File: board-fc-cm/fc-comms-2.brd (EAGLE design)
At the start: 95.9 x 90.2 mm, 230 parts, among them IC1 TPS79930QDDCRQ1, IC11 MPU-9250, IC12 TXB0108PW, IC13 TPS3813K33-EP_DBV_6, IC14 TMP100-EP_DBV_6, IC15 LHA1+, IC16 PCT2075TP, IC17 MMZ09332BT1, IC18 PCT2075TP, IC2 TPS79930QDDCRQ1, IC3 MSP430FR2311PW, IC4 MCP1700TT, IC5 TXB0108PW, IC6 TXB0108PW, IC7 CC1125RHBT, IC77 74LVC1G08, IC8 CC1125RHBT, IC9 TM4C123[7,G]XXPM, J3 SWD_SHROUD, Q3 32.768kHz, Q4 BSS123, Q5 BSS84, X1 SHIELD-26X26, X12 BU-SMA-V, X18 BU-SMA-V, X2 SHIELD-26X26, X3 LFTCXO070, X4 LFTCXO070, X5 SHIELD-26X26, X6 SHIELD-26X26, Y1 8MHz

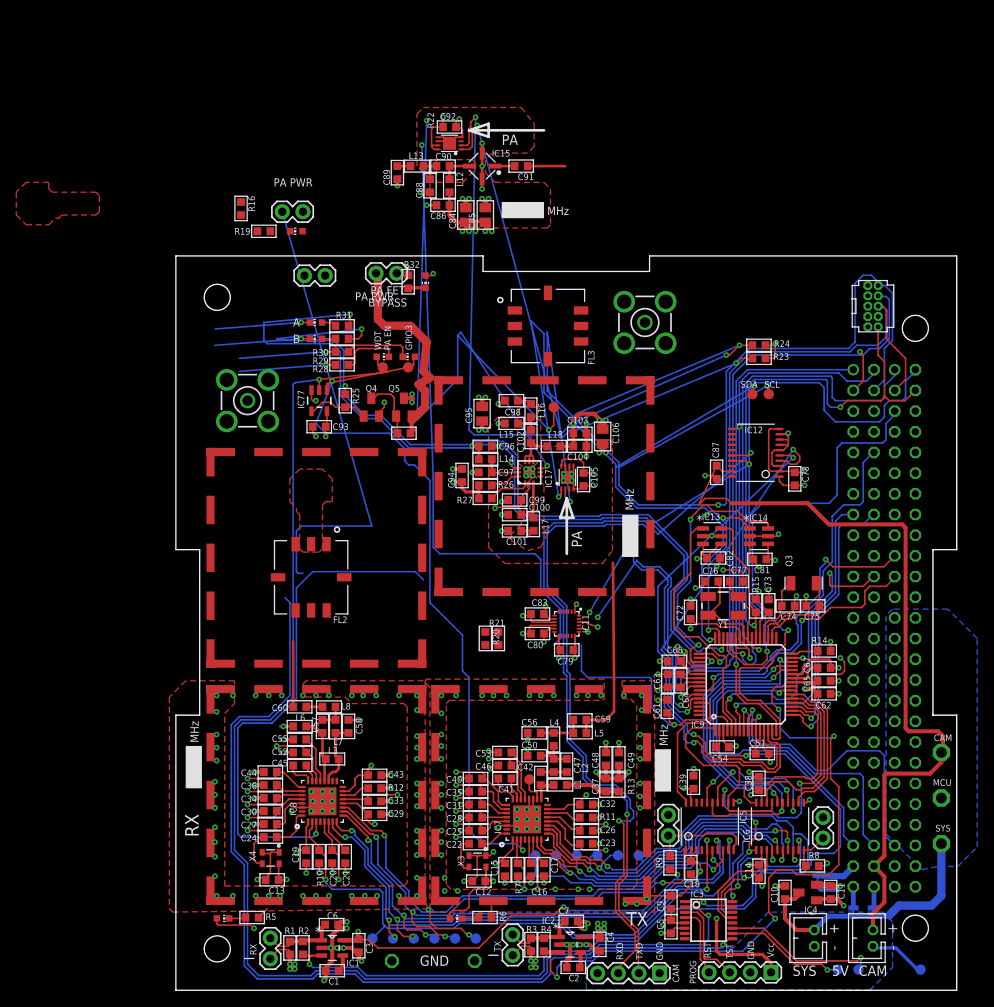
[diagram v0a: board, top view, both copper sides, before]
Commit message: adding fram, some routing
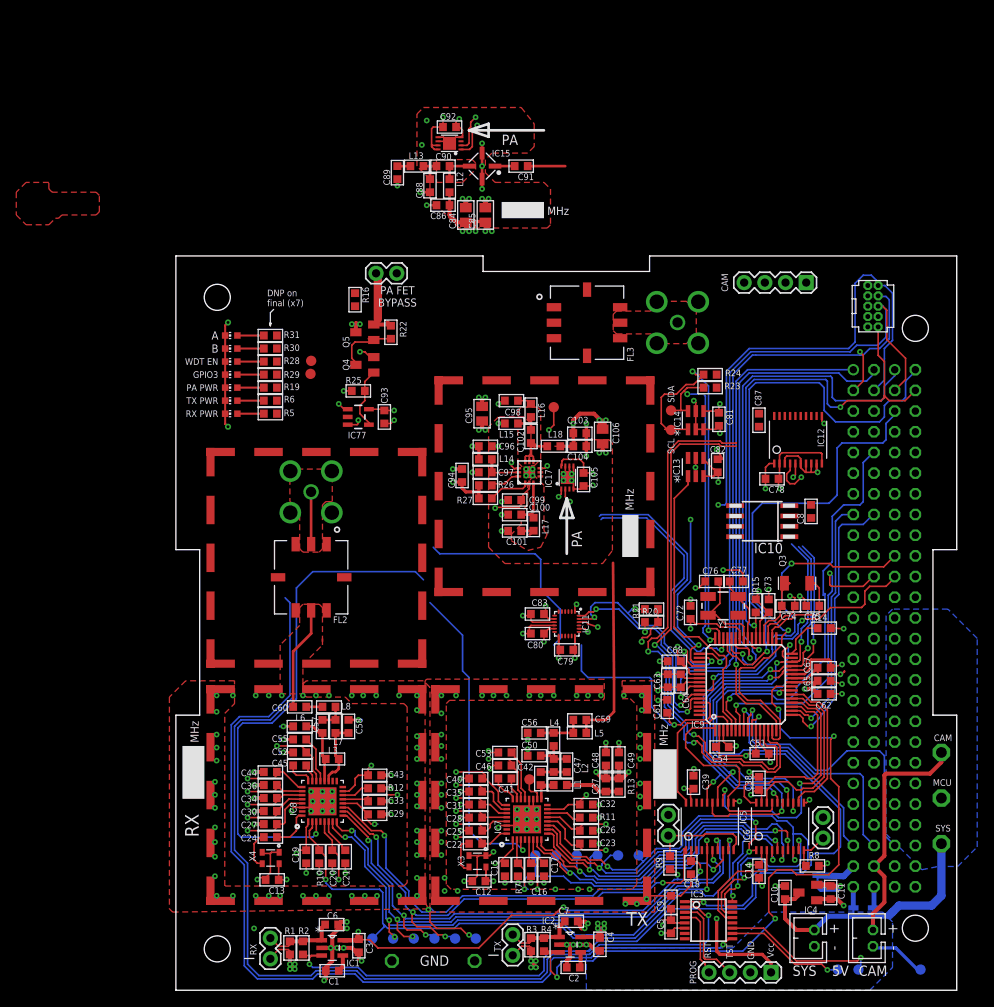
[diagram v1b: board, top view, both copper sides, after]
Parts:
- removed JP11, JP9: M02PTH, SparkFun-Connectors:1X02
- removed LED9: (no value), dtb:CHIP-LED0603
- removed R32: (no value), passives-7351:R0603-N
- added C8: 0.1u, passives-7351:C0603-N
- added IC10: FM25V10, cube-parts:SO-08M
- moved JP12 86.7 mm to (77.4, 86.9)
- moved LED1 69.3 mm to (6.80, 72.4), turned to 90 degrees
- moved R6 68.7 mm to (11.6, 72.4), turned to 180 degrees
- moved LED2 62.0 mm to (6.80, 70.8), turned to 90 degrees
- moved R5 61.9 mm to (11.6, 70.8), turned to 180 degrees
- moved LED6 21.9 mm to (6.80, 75.6)
- moved LED4 20.8 mm to (6.80, 74.0)
- moved R20 20.5 mm to (58.4, 45.2), turned to 0 degrees
- moved R19 19.2 mm to (11.6, 74.0), turned to 180 degrees
- moved R21 19.1 mm to (58.4, 46.8), turned to 0 degrees
- moved LED5 18.6 mm to (6.80, 77.2), turned to 90 degrees
- moved R16 17.9 mm to (22.0, 84.8)
- moved C81 17.9 mm to (66.7, 70.1), turned to 270 degrees
- moved IC14 16.2 mm to (63.8, 70.0), turned to 90 degrees
- moved X12 13.6 mm to (16.6, 61.2), flipped to the bottom
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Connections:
- removed net N$101: C60.2
- removed net N$24: C103.1, C104.1, C106.1, C94.1, C95.1, C96.1, C99.1, IC17.2, JP11.1, L14.2, L18.2, LED9.A, R26.1, R27.1
- removed net N$66: LED1.C, R6.1
- removed net N$67: LED2.C, R5.1
- removed net N$83: C84.1, C85.1, C86.2, JP9.1, L12.2, LED4.A
- removed net N$84: LED4.C, R19.1
- removed net N$85: LED9.C, R32.1
- new net FRAM_CS: IC10.1, IC9.53
- new net N$10: LED5.A, R28.1
- new net N$25: LED6.A, R29.1
- new net N$46: LED2.A, R5.2
- net 3V3/FMCU: now also C8.1, IC10.3, IC10.7, IC10.8
- net GND: now also C8.2, IC10.4, LED1.C, LED2.C, LED4.C, LED5.C, LED6.C; no longer R19.2, R28.1, R29.1, R32.2, R5.2, R6.2
- net N$38: now also LED4.A, R19.2; no longer LED5.C, R28.2
- net N$40: now also R6.1; no longer LED1.A
- net N$41: now also LED1.A, R6.2; no longer LED6.C, R29.2
- net N$53: now also R5.1; no longer LED2.A
- net N$56: now also C60.2
- net PA_PWR: now also C103.1, C104.1, C106.1, C84.1, C85.1, C86.2, C94.1, C95.1, C96.1, C99.1, IC17.2, L12.2, L14.2, L18.2, R19.1, R26.1, R27.1; no longer JP11.2, JP9.2
- net TC/TXRX/CLK: now also IC10.6
- net TC/TXRX/MISO: now also IC10.2
- net TC/TXRX/MOSI: now also IC10.5
- net TX_GPIO3: now also R29.2; no longer LED6.A
- net WDT_PA_EN: now also R28.2; no longer LED5.A
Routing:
- net TMP/SCL: track 206.5 -> 57.0 mm, vias 7 -> 4
- net PA_POWER: track 275.7 -> 140.8 mm
- net TMP/SDA: track 179.8 -> 46.7 mm, vias 6 -> 4
- net N$83: track 104.2 -> 0.00 mm, vias 5 -> 0
- net N$73: track 94.2 -> 0.00 mm, vias 2 -> 0
- net N$61: track 94.1 -> 0.00 mm, vias 2 -> 0
- net PA_PWR: track 72.8 -> 166.2 mm, vias 2 -> 14
- net N$24: track 89.3 -> 0.00 mm, vias 9 -> 1
- net N$49: track 103.5 -> 31.4 mm, vias 2 -> 1
- net N$51: track 100.3 -> 31.4 mm, vias 2 -> 1
- net 5V/CAM: track 95.9 -> 29.5 mm
- net GND: track 999.0 -> 1055.8 mm, vias 236 -> 232
- net WDT_PA_EN: track 159.8 -> 105.7 mm, vias 2 -> 1
- net TX_GPIO3: track 91.7 -> 40.6 mm
- net 5V/TX: track 38.4 -> 19.5 mm
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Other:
- board text added: "Comms/FC Board V.2"
- board text added: "DNP on final (x7)"
- board text added: "RX PWR"
- board text added: "TX PWR"
- board text added: "WDT EN"
- board text removed: "Comms/FC Development Board V.1"
- board text removed: "WDT PA EN"

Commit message: most routing done, still some queries remain
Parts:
- moved R16 1.26 mm to (22.4, 83.6), turned to 180 degrees
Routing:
- net GND: track 1055.8 -> 416.6 mm, vias 232 -> 234
- net 3V3/FMCU: track 288.4 -> 157.2 mm, vias 18 -> 21
- net PA_PWR: track 166.2 -> 71.6 mm, vias 14 -> 15
- net PA_POWER: track 140.8 -> 52.7 mm
- net N$51: track 31.4 -> 98.0 mm, vias 1 -> 2
- net N$49: track 31.4 -> 96.2 mm, vias 1 -> 2
- net RX_GPIO3: track 63.6 -> 1.53 mm
- net WDT_PA_EN: track 105.7 -> 164.5 mm, vias 1 -> 2
- net N$53: track 149.4 -> 192.9 mm, vias 18 -> 19
- net N$1: track 115.6 -> 158.4 mm, vias 1 -> 2
- net FRAM_CS: track 0.00 -> 42.6 mm, vias 0 -> 2
- net TX_GPIO3: track 40.6 -> 80.9 mm, vias 2 -> 3
- net TMP/SDA: track 46.7 -> 66.4 mm, vias 4 -> 6
- net TMP/SCL: track 57.0 -> 76.2 mm, vias 4 -> 6
- net 5V/CAM: track 29.5 -> 47.0 mm
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- added copper zone on layer 1, net 5V/CAM
- added copper zone on layer 1, net N$2
- removed copper zone on layer 16, net 5V/CAM
- removed copper zone on layer 15, net N$2
- removed copper zone on layer 15, net N$24

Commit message: added camera header, RF connectors, some cleanup
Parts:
- removed JP12: (no value), SparkFun-Connectors:1X04
- removed JP13, JP14, JP4: JUMPER-SMT_2_NC_TRACE_SILK, SparkFun-Jumpers:SMT-JUMPER_2_NC_TRACE_SILK
- removed X12, X18: BU-SMA-V, con-coax:BU-SMA-V
- added JP7: B4B-PH-K-S, cube-parts:B4B-PH-K-S
- added JP8, JP9: MCX, cube-parts:MCX-STRAIGHT
- added R17, R18: 1k, passives-7351:R0603-N
- added SJ1, SJ2, SJ3: JUMPER-PAD-2-NOYES_SILK, SparkFun-Passives:PAD-JUMPER-2-NO_YES_SILK
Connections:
- removed net N$61: IC12.17, JP12.3
- removed net N$73: IC12.16, JP12.2
- new net N$50: IC12.17, R17.2
- new net N$52: IC12.16, R18.2
- net 3V3/FMCU: now also SJ3.2; no longer JP4.2
- net 5V/CAM: now also JP7.1; no longer JP12.4
- net 5V/RX: now also SJ1.2; no longer JP14.2
- net 5V/SYS: now also SJ1.1, SJ2.1; no longer JP13.1, JP14.1
- net 5V/TX: now also SJ2.2; no longer JP13.2
- net GND: now also JP7.2, JP8.P$2, JP8.P$3, JP8.P$4, JP8.P$5, JP9.P$2, JP9.P$3, JP9.P$4, JP9.P$5; no longer JP12.1, X12.2, X12.3, X12.4, X12.5, X18.2, X18.3, X18.4, X18.5
- net N$29: now also JP8.P$1; no longer X18.1
- net N$55: now also JP9.P$1; no longer X12.1
- net N$64: now also SJ3.1; no longer JP4.1
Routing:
- net GND: track 416.6 -> 328.6 mm, vias 234 -> 338
- net 3V3/FMCU: track 157.2 -> 134.8 mm
- net PA_POWER: track 52.7 -> 70.9 mm
- net N$73: track 14.5 -> 0.00 mm
- net N$61: track 13.9 -> 0.00 mm
- net N$40: track 216.2 -> 220.9 mm
- net N$53: track 192.9 -> 196.7 mm
- net N$50: track 0.00 -> 3.74 mm
- net N$52: track 0.00 -> 3.62 mm
- net N$23: track 23.7 -> 26.7 mm
- net N$5: track 31.0 -> 32.5 mm
- net TX_GPIO3: track 80.9 -> 79.7 mm
- net N$34: track 9.23 -> 8.31 mm
- net ANT/GATE: track 38.9 -> 38.3 mm
- net ANT/SW: track 33.2 -> 32.7 mm
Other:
- board text added: "?X"
- board text added: "CAMERA"
- board text added: "Comms/FC Board V.3"
- board text added: "L1"
- board text added: "L4"
- board text added: "Oct'18"
- board text removed: "Comms/FC Board V.2"
- board text removed: "Mar'17"

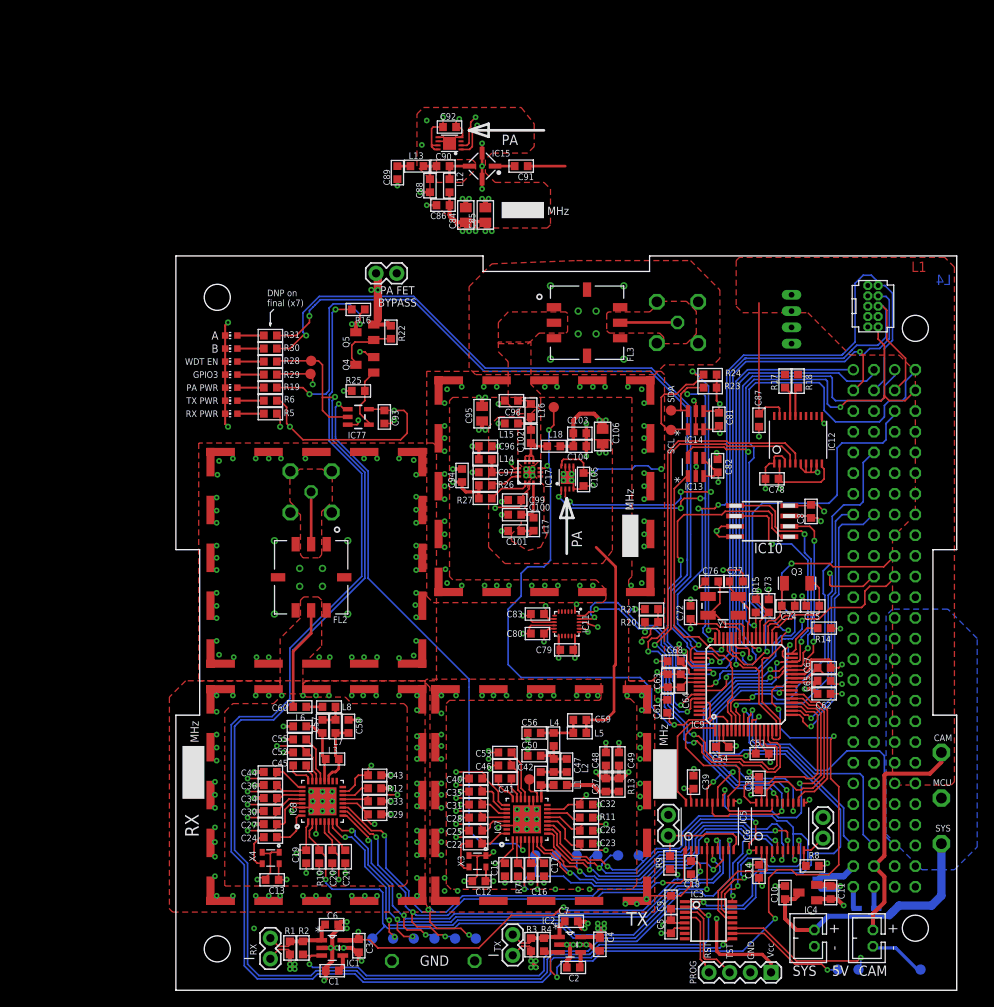
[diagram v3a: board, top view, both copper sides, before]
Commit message: switching to lha1+, camera rx/tx done
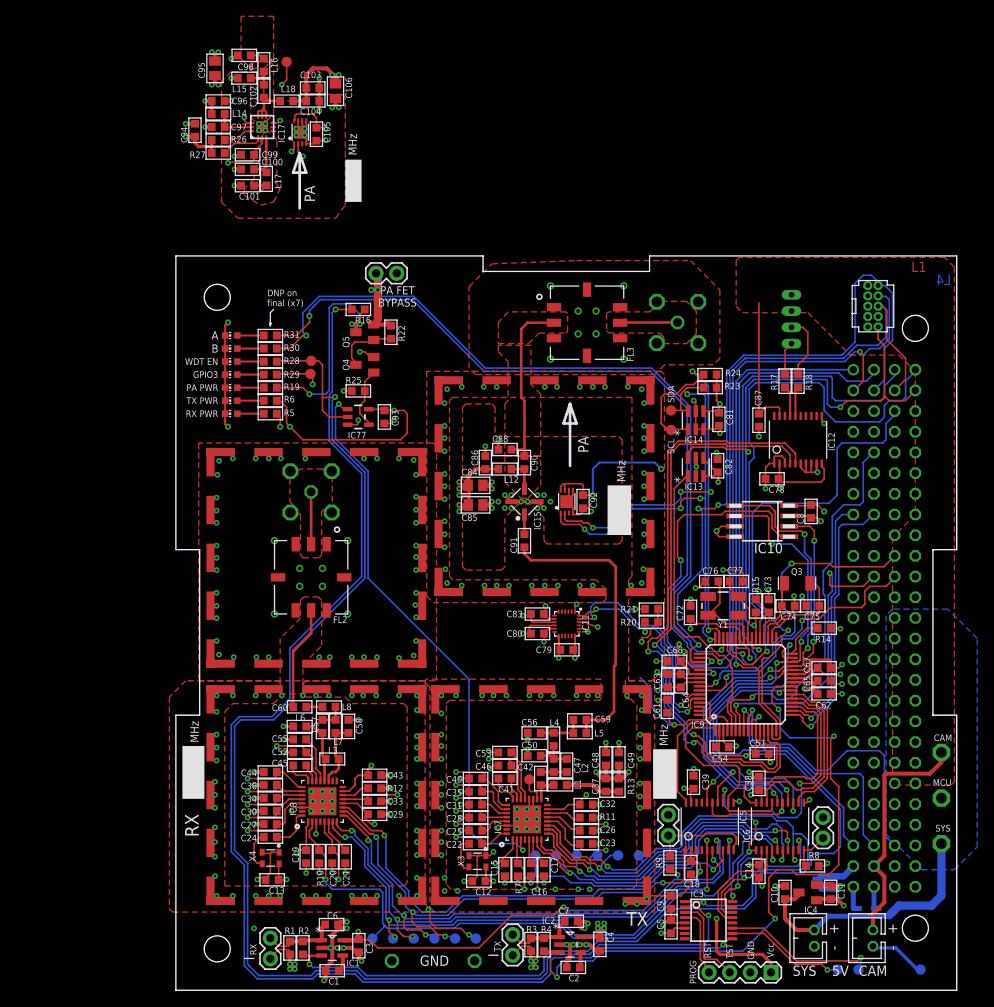
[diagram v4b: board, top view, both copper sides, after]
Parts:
- removed C89: dnp, passives-7351:C0603-N
- removed L13: 0R, passives-7351:L0603-N
- moved C95 53.6 mm to (4.80, 113.2)
- moved L15 53.6 mm to (8.40, 112.0)
- moved C100 53.6 mm to (8.80, 100.8)
- moved C101 53.6 mm to (8.80, 98.8)
- moved C102 53.6 mm to (10.8, 110.4)
- moved C104 53.6 mm to (16.8, 109.2)
- moved C105 53.6 mm to (17.3, 105.1)
- moved C106 53.6 mm to (19.6, 110.4)
- moved C94 53.6 mm to (2.34, 105.6)
- moved C96 53.6 mm to (5.20, 109.2)
- moved C97 53.6 mm to (5.20, 106.0)
- moved C98 53.6 mm to (8.40, 114.8)
- moved IC17 53.6 mm to (10.6, 106.0)
- moved IC18 53.6 mm to (15.3, 105.4)
- moved L17 53.6 mm to (11.1, 99.6)
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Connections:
- removed net N$28: FL3.2
- removed net N$37: C89.2, L13.2
- new net N$24: JP7.3, R18.1
- net GND: no longer C89.1
- net N$23: now also C91.1
- net N$26: now also JP7.4, R17.1; no longer C91.1
- net N$27: now also FL3.2; no longer L13.1
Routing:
- net PA_POWER: track 70.9 -> 21.7 mm, vias 5 -> 3
- net N$27: track 3.20 -> 21.7 mm
- net N$23: track 26.7 -> 36.0 mm
- net N$24: track 0.00 -> 7.95 mm
- net 3V3/FMCU: track 134.8 -> 138.1 mm
- net TMP/SDA: track 66.4 -> 64.1 mm
- net TMP/SCL: track 76.2 -> 74.4 mm
- net N$37: track 1.66 -> 0.00 mm
- net GND: track 328.6 -> 327.7 mm, vias 338 -> 346
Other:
- board text removed: "?X"
